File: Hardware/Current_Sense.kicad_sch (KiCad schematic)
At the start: 37 parts, among them IC2 INA241A4IDR, IC3 AMC1350DWVR, IC6 TLV9002QDRQ1, J6 Scrut Conn, SW3 Scrut Select, U9 REF35125QDBVR

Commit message: some comments so I don't forget what I'm doing
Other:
- note added: "Convert to SPST switch? (Scrut- = Shunt-) Also, pass scrut thru INA or directly to ADC?"
- note added: "Make sure common-mode stuff is within range"
- note added: "Verify op-amp"
- note added: "Vref = GND?"
- note removed: "Convert to SPST switch? (Scrut- = Shunt-)"
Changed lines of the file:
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@@
 		)
 	)
+	(text "Make sure common-mode stuff is within range"
+		(exclude_from_sim no)
+		(at 81.28 160.274 0)
+		(effects
+			(font
+				(size 1.27 1.27)
+				(color 255 8 29 1)
+			)
+			(justify left top)
+		)
+	)
 	(text "-->"
 		(exclude_from_sim no)
@@
 		)
 	)
+	(text "Verify op-amp"
+		(exclude_from_sim no)
+		(at 240.284 159.512 0)
+		(effects
+			(font
+				(size 1.27 1.27)
+				(color 255 8 29 1)
+			)
+			(justify left top)
+		)
+	)
 	(text "Current = ( (ADC * (3.3 / 4096) - Vref) / (Shunt*gain) )\n\nVref = 1.25\nShunt * gain = 250u * 100 V/V = 0.025\n"
 		(exclude_from_sim no)
@@
 		)
 	)
+	(text "Vref = GND?"
+		(exclude_from_sim no)
+		(at 221.996 138.938 0)
+		(effects
+			(font
+				(size 1.27 1.27)
+				(color 255 8 29 1)
+			)
+			(justify left top)
+		)
+	)
 	(text "Low-side shunt, so current path is as follows:\n* Discharge: Output_GND -> Battery_GND\n* Charge: Battery_GND -> Output_GND"
 		(exclude_from_sim no)
@@
 		)
 	)
-	(text "Convert to SPST switch? (Scrut- = Shunt-) "
+	(text "Convert to SPST switch? (Scrut- = Shunt-) \nAlso, pass scrut thru INA or directly to ADC?"
 		(exclude_from_sim no)
-		(at 162.306 57.404 0)
+		(at 158.75 56.388 0)
 		(effects
 			(font
@@
 	)
 	(junction
+		(at 115.57 138.43)
+		(diameter 0)
+		(color 0 0 0 0)
+	)
+	(junction
 		(at 208.28 121.92)
 		(diameter 0)
@@
 	)
 	(junction
-		(at 119.38 138.43)
-		(diameter 0)
-		(color 0 0 0 0)
-	)
-	(junction
 		(at 208.28 127)
 		(diameter 0)
@@
 	)
 	(junction
-		(at 121.92 138.43)
-		(diameter 0)
-		(color 0 0 0 0)
-	)
-	(junction
 		(at 265.43 127)
 		(diameter 0)
@@
 	)
 	(junction
+		(at 121.92 130.81)
+		(diameter 0)
+		(color 0 0 0 0)
+	)
+	(junction
 		(at 57.15 128.27)
 		(diameter 0)
@@
 	(wire
 		(pts
+			(xy 121.92 130.81) (xy 121.92 132.08)
+		)
+		(stroke
+			(width 0)
+			(type default)
+		)
+	)
+	(wire
+		(pts
 			(xy 49.53 82.55) (xy 49.53 83.82)
 		)
@@
 	(wire
 		(pts
-			(xy 168.91 50.8) (xy 176.53 50.8)
+			(xy 115.57 138.43) (xy 119.38 138.43)
 		)
 		(stroke
@@
 	(wire
 		(pts
-			(xy 119.38 138.43) (xy 121.92 138.43)
+			(xy 168.91 50.8) (xy 176.53 50.8)
 		)
 		(stroke
@@
 	(wire
 		(pts
-			(xy 110.49 138.43) (xy 119.38 138.43)
+			(xy 110.49 138.43) (xy 115.57 138.43)
 		)
 		(stroke
@@
 	(wire
 		(pts
-			(xy 121.92 132.08) (xy 121.92 138.43)
-		)
-		(stroke
-			(width 0)
-			(type default)
-		)
-	)
-	(wire
-		(pts
 			(xy 217.17 140.97) (xy 220.98 140.97)
 		)
@@
 	(symbol
 		(lib_id "power:GND")
-		(at 121.92 138.43 0)
+		(at 115.57 138.43 0)
 		(unit 1)
 		(exclude_from_sim no)
@@
 		(fields_autoplaced yes)
 		(property "Reference" "#PWR0111"
-			(at 121.92 144.78 0)
+			(at 115.57 144.78 0)
 			(effects
 				(font
@@
 		)
 		(property "Value" "GND HV"
-			(at 121.92 143.51 0)
+			(at 115.57 143.51 0)
 			(effects
 				(font
@@
 		)
 		(property "Footprint" ""
-			(at 121.92 138.43 0)
+			(at 115.57 138.43 0)
 			(effects
 				(font
@@
 		)
 		(property "Datasheet" ""
-			(at 121.92 138.43 0)
+			(at 115.57 138.43 0)
 			(effects
 				(font
@@
 		)
 		(property "Description" "Power symbol creates a global label with name \"GND\" , ground"
-			(at 121.92 138.43 0)
+			(at 115.57 138.43 0)
 			(effects
 				(font

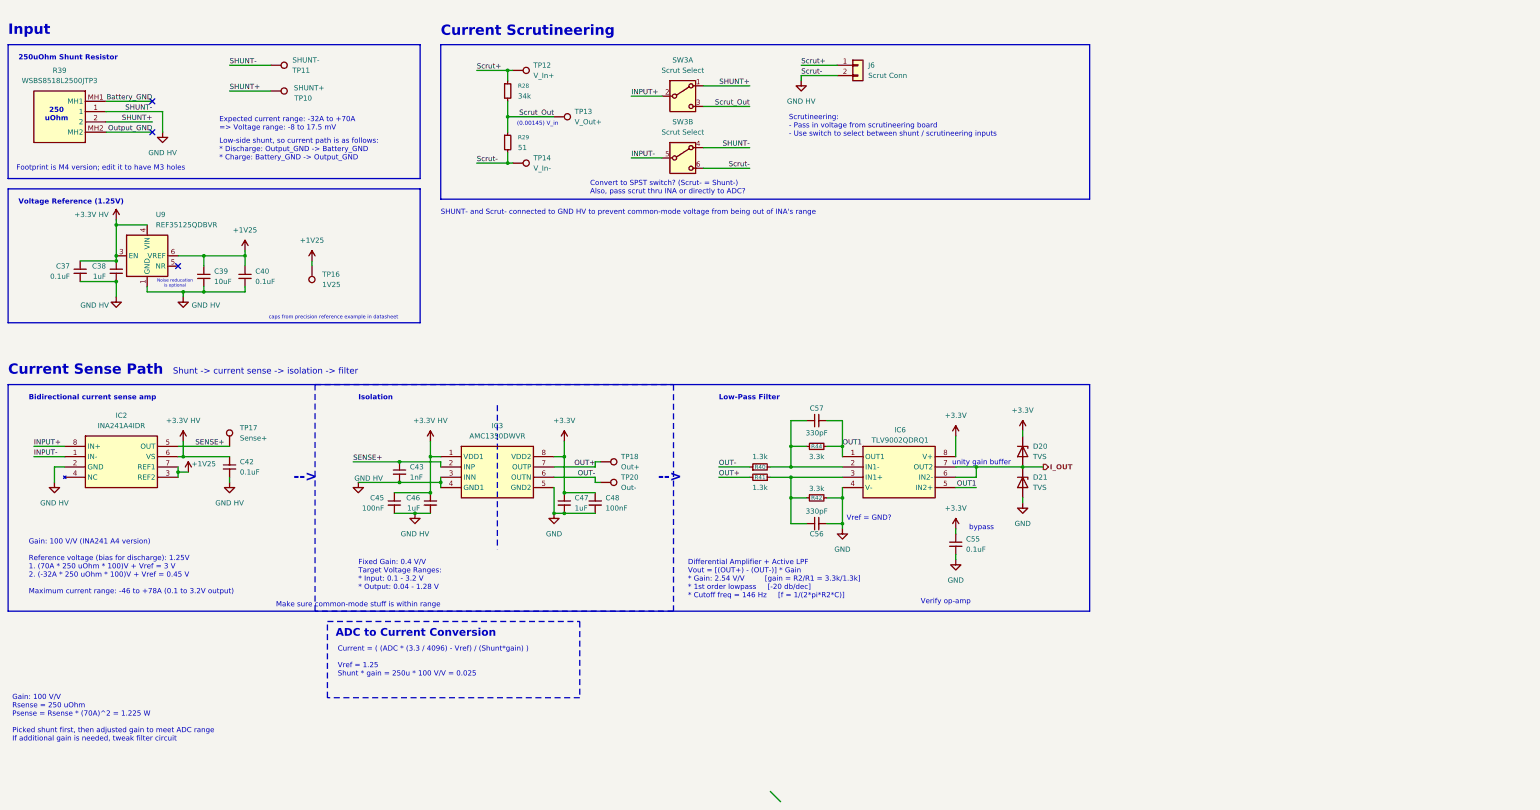
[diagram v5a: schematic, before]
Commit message: new TLV symbol, SPDT switch for scrut
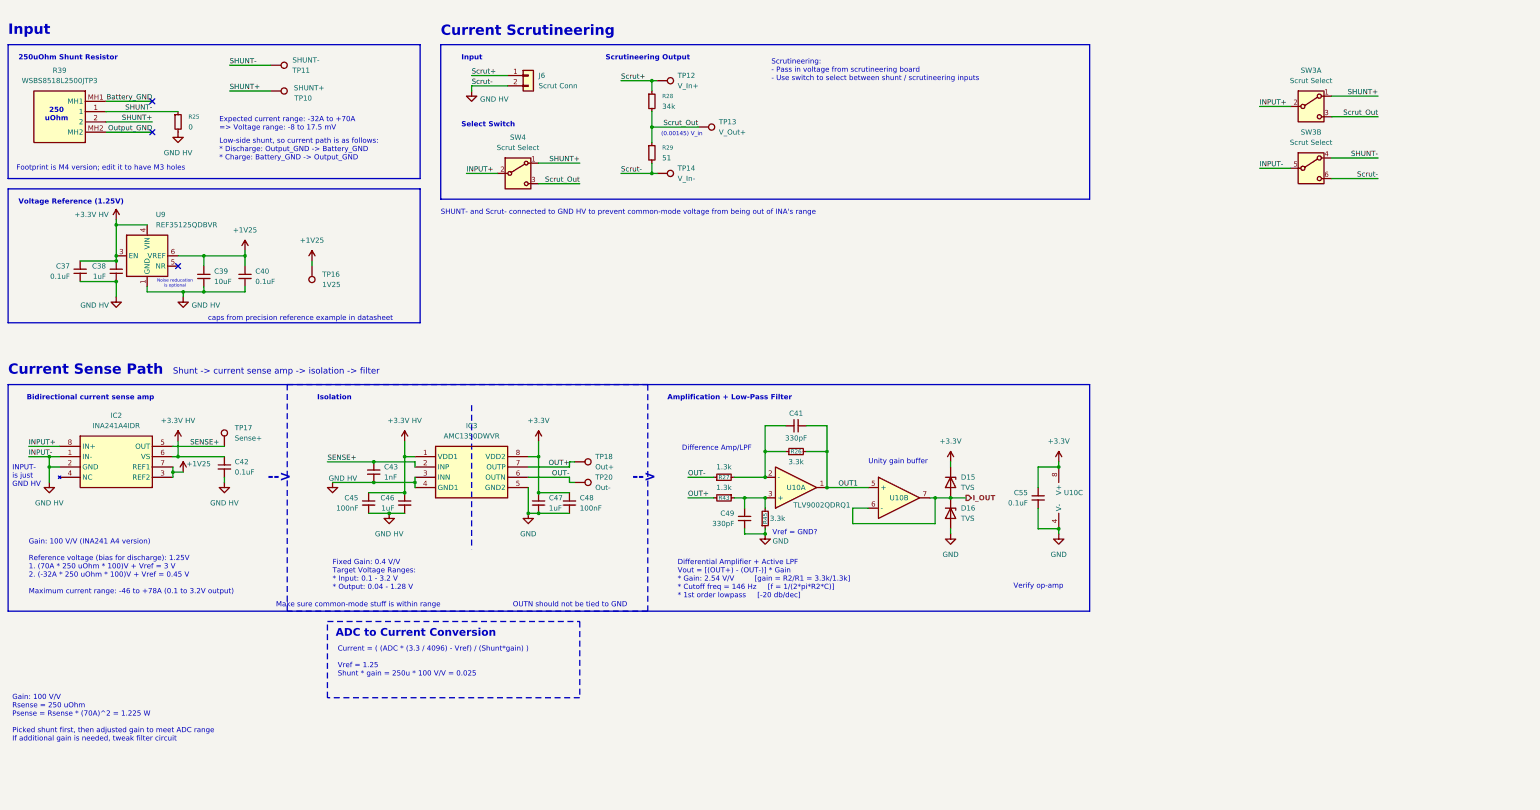
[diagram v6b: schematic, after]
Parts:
- removed C56, C57: 330pF, Capacitor_SMD:C_0603_1608Metric_Pad1.08x0.95mm_HandSolder, symbol Device:C_Small
- removed D20, D21: TVS, Diode_SMD:D_SOD-123F, symbol Device:D_Zener
- removed IC6: TLV9002QDRQ1, Parts:TLV9002QDRQ1, symbol TLV9002QDRQ1:TLV9002QDRQ1
- removed R40, R41: 1.3k, symbol Device:R_Small
- removed R42, R44: 3.3k, symbol Device:R_Small
- added C41, C49: 330pF, Capacitor_SMD:C_0603_1608Metric_Pad1.08x0.95mm_HandSolder, symbol Device:C_Small
- added D15, D16: TVS, Diode_SMD:D_SOD-123F, symbol Device:D_Zener
- added R25: 0, symbol Device:R_Small
- added R26, R45: 3.3k, symbol Device:R_Small
- added R27, R43: 1.3k, symbol Device:R_Small
- added SW4: Scrut Select, symbol Switch:SW_SPDT
- added U10: TLV9002QDRQ1, Package_SO:SOIC-8_3.9x4.9mm_P1.27mm, symbol utsvt-misc:TLV9002QDRQ1
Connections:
- net INPUT- is gone; now on net GND HV: IC2.1 (IN-), SW3.5 (B)
- net +3.3V: now also D15.1 (K), U10.8 (V+)
- net GND: now also C49.2, D16.2 (A), R45.1, U10.4 (V-)
- net GND HV: now also R25.2; no longer R39.1, SW3.4 (A), TP11.1
- net INPUT+: now also SW4.2 (B)
- net I_OUT: now also D15.2 (A), D16.1 (K), U10.6 (-), U10.7
- net OUT+: now also R43.2
- net OUT-: now also R27.1
- net OUT1: now also C41.2, R26.2, U10.1, U10.5 (+)
- net SHUNT+: now also SW4.1 (A)
- net Scrut_Out: now also SW4.3 (C)
- new net: C49.1, R43.1, R45.2, U10.3 (+)
- new net: C41.1, R26.1, R27.2, U10.2 (-)
- new net SHUNT-: R25.1, R39.1, SW3.4 (A), TP11.1
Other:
- note added: "Amplification + Low-Pass Filter"
- note added: "Difference Amp/LPF"
- note added: "Differential Amplifier + Active LPF Vout = [(OUT+) - (OUT-)] * Gain * Gain: 2.54 V/V [gain = R2/R1 = 3.3k/1.3k] * Cutoff freq = 146 Hz [f = 1/(2*pi*R2*C)] * 1st order lowpass [-20 db/dec]"
- note added: "INPUT- is just GND HV"
- note added: "OUTN should not be tied to GND"
- note added: "Scrutineering Output"
- note added: "Select Switch"
- note added: "Shunt -> current sense amp -> isolation -> filter"
- note added: "Unity gain buffer"
- note removed: "Convert to SPST switch? (Scrut- = Shunt-) Also, pass scrut thru INA or directly to ADC?"
- note removed: "Differential Amplifier + Active LPF Vout = [(OUT+) - (OUT-)] * Gain * Gain: 2.54 V/V [gain = R2/R1 = 3.3k/1.3k] * 1st order lowpass [-20 db/dec] * Cutoff freq = 146 Hz [f = 1/(2*pi*R2*C)]"
- note removed: "Low-Pass Filter"
- note removed: "Shunt -> current sense -> isolation -> filter"
- note removed: "bypass"
- note removed: "unity gain buffer"
- moved on the sheet: C42, C43, C45, C46, C47, C48, C55, IC2, IC3, J6, R28, R29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

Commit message: fixed LPF cutoff
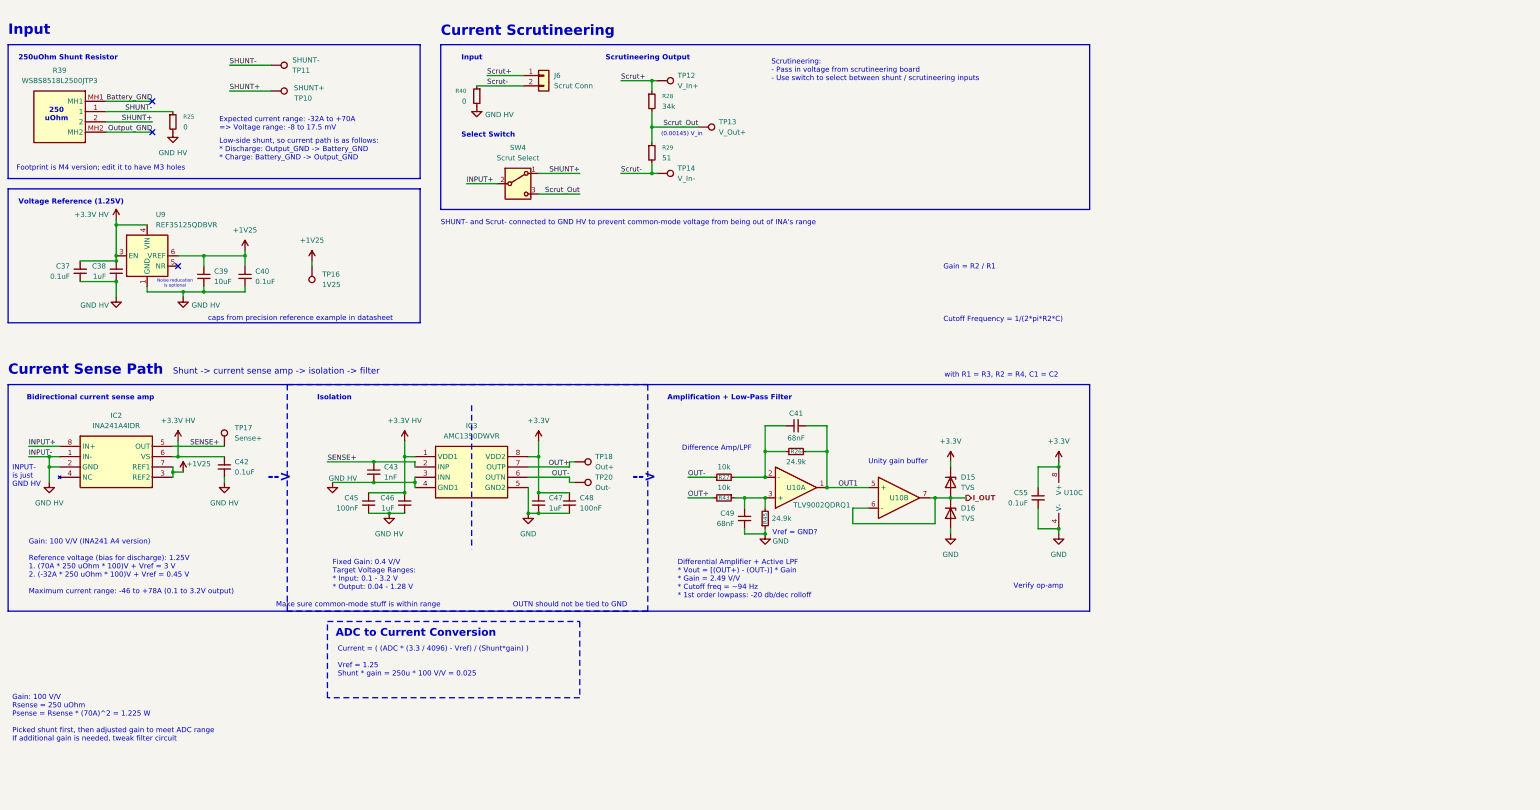
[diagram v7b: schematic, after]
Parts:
- removed SW3: Scrut Select, Parts:CAS220TB, symbol Switch:SW_DPDT_x2
- added R40: 0, symbol Device:R_Small
- C41, C49: value 330pF -> 68nF
- R26, R45: value 3.3k -> 24.9k
- R27, R43: value 1.3k -> 10k
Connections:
- net GND HV: now also R40.2; no longer J6.2 (Pin_2), R29.2, TP14.1
- new net Scrut-: J6.2 (Pin_2), R29.2, R40.1, TP14.1
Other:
- note added: "Cutoff Frequency = 1/(2*pi*R2*C)"
- note added: "Differential Amplifier + Active LPF * Vout = [(OUT+) - (OUT-)] * Gain * Gain = 2.49 V/V * Cutoff freq = ~94 Hz * 1st order lowpass: -20 db/dec rolloff"
- note added: "Gain = R2 / R1"
- note added: "with R1 = R3, R2 = R4, C1 = C2"
- note removed: "Differential Amplifier + Active LPF Vout = [(OUT+) - (OUT-)] * Gain * Gain: 2.54 V/V [gain = R2/R1 = 3.3k/1.3k] * Cutoff freq = 146 Hz [f = 1/(2*pi*R2*C)] * 1st order lowpass [-20 db/dec]"
- moved on the sheet: J6, R25, SW4
